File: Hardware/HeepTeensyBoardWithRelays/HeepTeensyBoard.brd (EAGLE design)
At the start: 100 x 54 mm, 47 parts, among them J1 MAGJACK, J4 POWER_JACKPTH, K1 RELAY-SPDT-JZC-11F, K2 RELAY-SPDT-JZC-11F, K3 RELAY-SPDT-JZC-11F, Q1 25MHz, U1 ENC28J60-SO

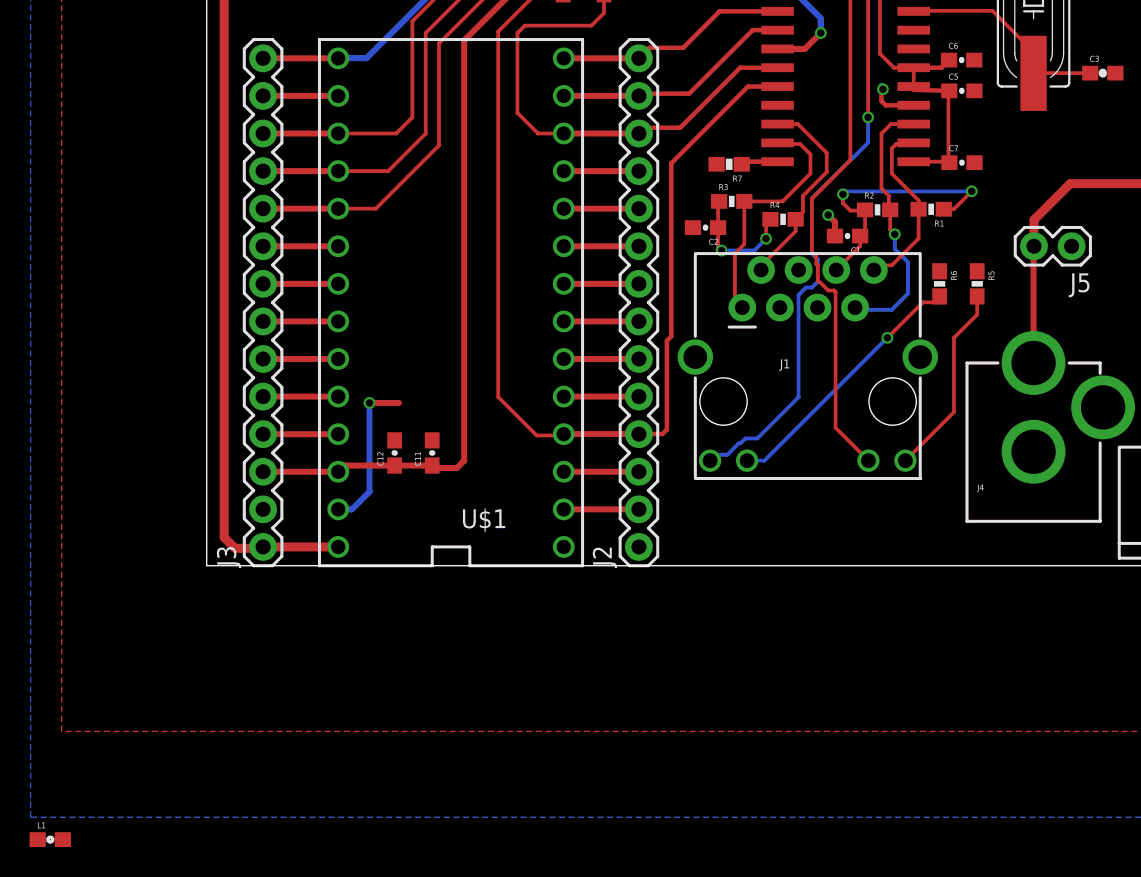
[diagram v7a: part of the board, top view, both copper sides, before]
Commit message: #156 Added ferrite bead to layout
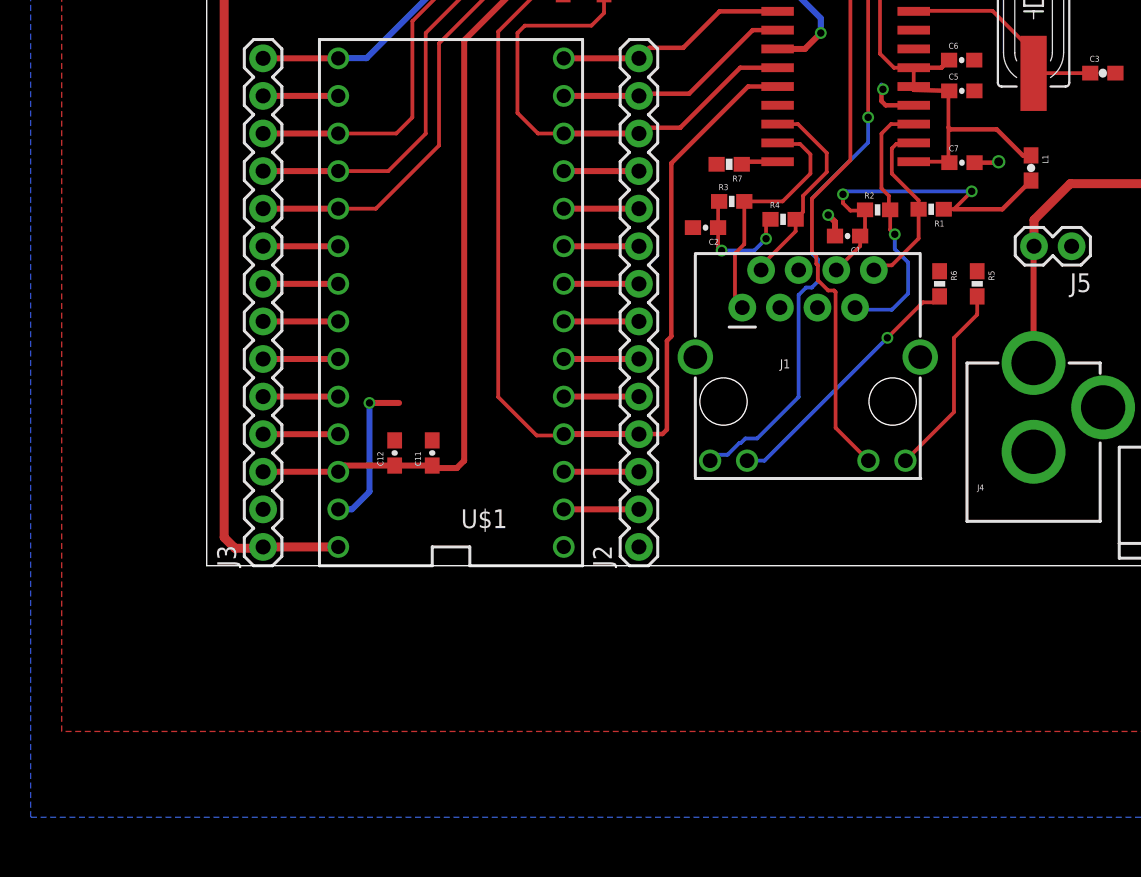
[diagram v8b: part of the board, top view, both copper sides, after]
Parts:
- moved L1 80.3 mm to (55.7, 26.9), turned to 270 degrees
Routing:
- net 3.3V: track 114.6 -> 121.0 mm
- net N$7: track 18.3 -> 24.4 mm
- net GND: track 15.9 -> 17.9 mm, vias 3 -> 4
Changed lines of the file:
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@@
 <attribute name="PROD_ID" value="DIO-08378" x="81.57" y="36.03" size="1.778" layer="27" display="off"/>
 </element>
-<element name="L1" library="SparkFun-Passives" package="0603" value="" x="-10.57" y="-18.51"/>
+<element name="L1" library="SparkFun-Passives" package="0603" value="" x="55.71" y="26.88" rot="R270"/>
 </elements>
 <signals>
@@
 <wire x1="44.44" y1="24" x2="44.49" y2="24.05" width="0.254" layer="1"/>
 <contactref element="L1" pad="2"/>
-<wire x1="-9.72" y1="-18.51" x2="42.545" y2="19.985" width="0" layer="19" extent="1-1"/>
+<wire x1="50.49" y1="24.09" x2="53.77" y2="24.09" width="0.3048" layer="1"/>
+<wire x1="53.77" y1="24.09" x2="55.71" y2="26.03" width="0.3048" layer="1"/>
 </signal>
 <signal name="GND">
@@
 <via x="11" y="11" extent="1-16" drill="0.5" shape="square"/>
 <wire x1="11" y1="11" x2="13" y2="11" width="0.4064" layer="1"/>
+<wire x1="51.89" y1="27.24" x2="53.46" y2="27.24" width="0.3048" layer="1"/>
+<wire x1="53.46" y1="27.24" x2="53.52" y2="27.3" width="0.3048" layer="1"/>
+<via x="53.52" y="27.3" extent="1-16" drill="0.6" shape="square"/>
+<wire x1="53.52" y1="27.3" x2="53.68" y2="27.3" width="0.3048" layer="16"/>
+<wire x1="53.68" y1="27.3" x2="53.81" y2="27.17" width="0.3048" layer="16"/>
 </signal>
 <signal name="LEDA">
@@
 <wire x1="50.125" y1="27.305" x2="50.19" y2="27.24" width="0.254" layer="1"/>
 <wire x1="47.78" y1="32.385" x2="47.78" y2="33.655" width="0.254" layer="1"/>
-<wire x1="50.125" y1="27.305" x2="50.125" y2="32.105" width="0.254" layer="1"/>
+<wire x1="50.125" y1="27.305" x2="50.125" y2="29.62" width="0.254" layer="1"/>
+<wire x1="50.125" y1="29.62" x2="50.125" y2="32.105" width="0.254" layer="1"/>
 <wire x1="50.125" y1="32.105" x2="50.18" y2="32.09" width="0.254" layer="1"/>
 <wire x1="47.78" y1="33.655" x2="46.445" y2="33.655" width="0.254" layer="1"/>
@@
 <wire x1="8.89" y1="6.35" x2="3.81" y2="6.35" width="0.4064" layer="1"/>
 <contactref element="L1" pad="1"/>
-<wire x1="3.81" y1="6.35" x2="-11.42" y2="-18.51" width="0" layer="19" extent="1-1"/>
+<wire x1="55.71" y1="27.73" x2="55.15" y2="27.73" width="0.3048" layer="1"/>
+<wire x1="55.15" y1="27.73" x2="53.39" y2="29.49" width="0.3048" layer="1"/>
+<wire x1="53.39" y1="29.49" x2="50.255" y2="29.49" width="0.3048" layer="1"/>
+<wire x1="50.255" y1="29.49" x2="50.125" y2="29.62" width="0.3048" layer="1"/>
 </signal>
 <signal name="N$15">
